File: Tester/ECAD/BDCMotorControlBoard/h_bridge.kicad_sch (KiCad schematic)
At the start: 70 parts, among them Q10 IRLR8726, Q11 IRLR8726, Q2 BC846, Q3 BC846BPN, Q4 BC846, Q5 BC846, Q6 BC846, Q7 BC846, Q8 IRLR8726, Q9 IRLR8726, U5 INA180A2, U6 IR2103, U7 IR2103

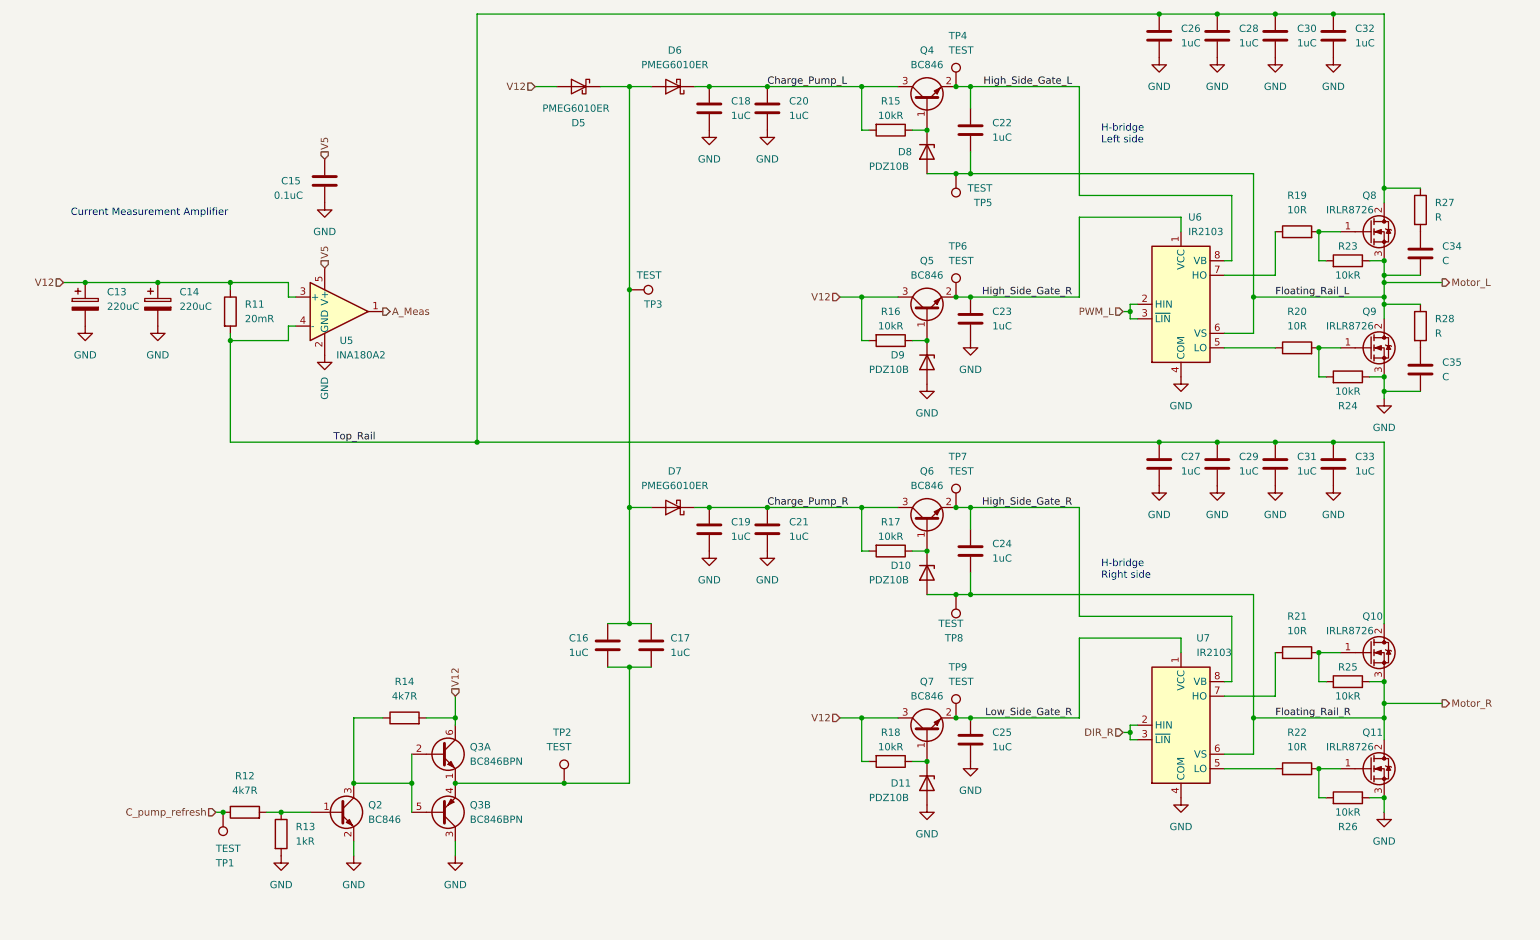
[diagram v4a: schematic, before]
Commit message: Update h_bridge.kicad_sch
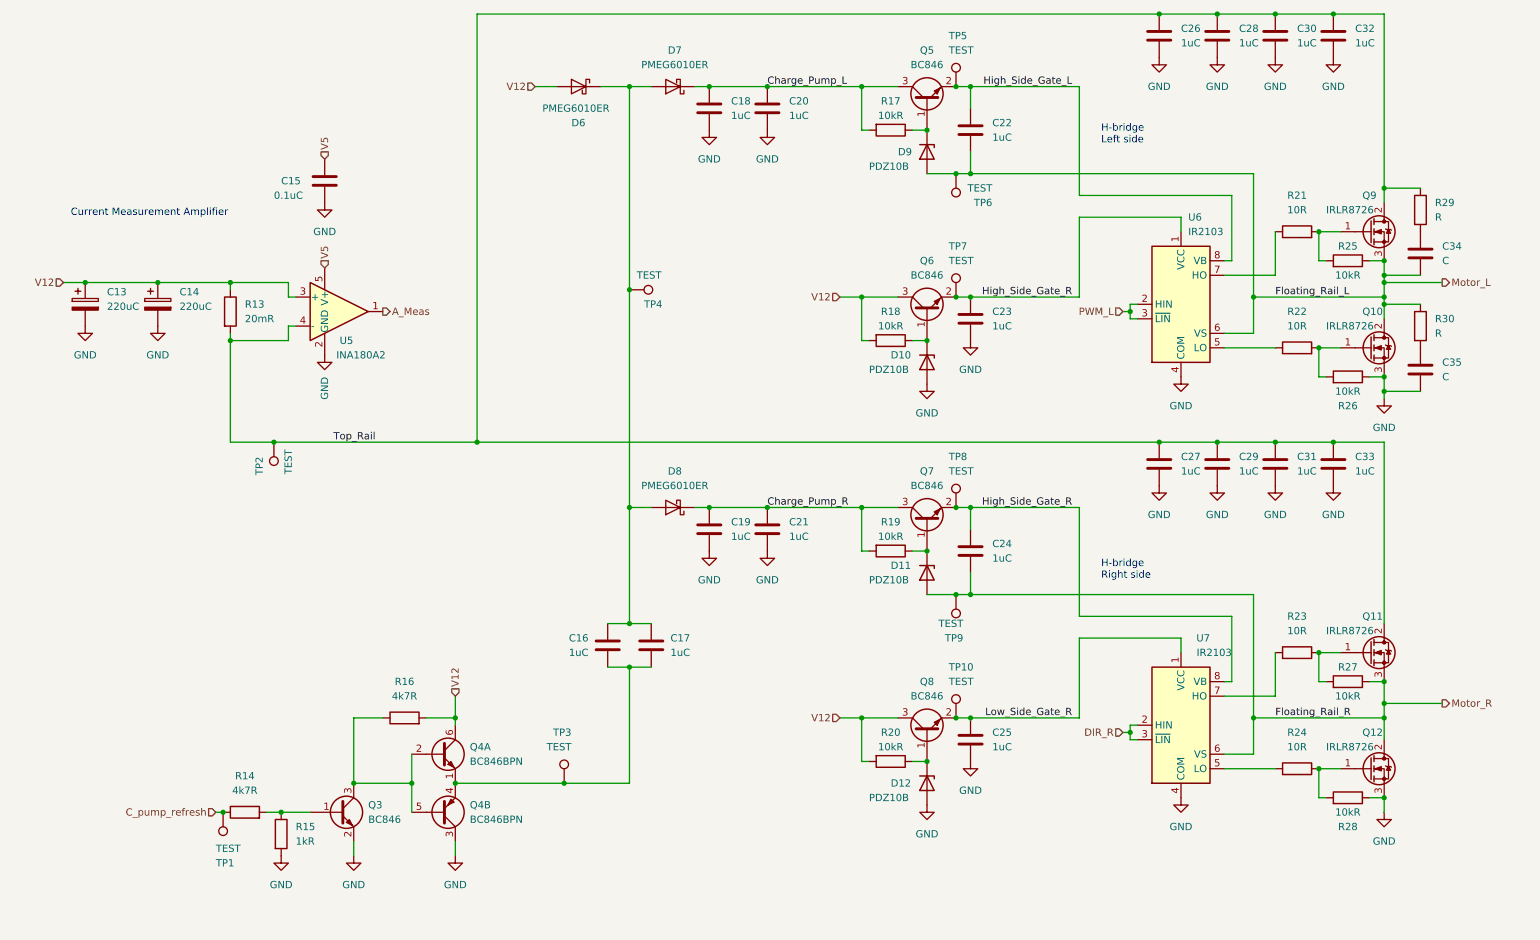
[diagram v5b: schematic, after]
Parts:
- added TP2: TEST, TestPoint:TestPoint_Pad_D1.5mm, symbol Connector:TestPoint
- renumbered D9 to D10, D10 to D11, D11 to D12, D5 to D6, D6 to D7, D7 to D8, D8 to D9, Q9 to Q10, Q10 to Q11, Q11 to Q12, Q2 to Q3, Q3 to Q4, Q4 to Q5, Q5 to Q6, Q6 to Q7, Q7 to Q8, Q8 to Q9, R11 to R13, R12 to R14, R13 to R15, R14 to R16, R15 to R17, R16 to R18, R17 to R19, R18 to R20, R19 to R21, R20 to R22, R21 to R23, R22 to R24, R23 to R25, R24 to R26, R25 to R27, R26 to R28, R27 to R29, R28 to R30, TP9 to TP10, TP2 to TP3, TP3 to TP4, TP4 to TP5, TP5 to TP6, TP6 to TP7, TP7 to TP8, TP8 to TP9
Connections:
- net Top_Rail: now also TP2.1

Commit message: Progressed CAD
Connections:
- net High_Side_Gate_R: no longer C23.1, Q6.2 (E), TP7.1, U6.1 (VCC)
- new net Low_Side_Gate_L: C23.1, Q6.2 (E), TP7.1, U6.1 (VCC)
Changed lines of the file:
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@@
     (effects (font (size 1.27 1.27)) (justify right bottom))
   )
-  (label "High_Side_Gate_R" (at 205.74 67.31 180)
+  (label "Low_Side_Gate_L" (at 205.74 67.31 180)
     (effects (font (size 1.27 1.27)) (justify right bottom))
-  )
-  (label "Floating_Rail_L" (at 241.3 67.31 0)
-    (effects (font (size 1.27 1.27)) (justify left bottom))
   )
   (label "Low_Side_Gate_R" (at 205.74 140.97 180)
@@
     (effects (font (size 1.27 1.27)) (justify left bottom))
   )
-  (label "Floating_Rail_R" (at 241.3 140.97 0)
-    (effects (font (size 1.27 1.27)) (justify left bottom))
-  )

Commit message: Progressed CAD
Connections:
- net Top_Rail: now also C13.1, C14.1
- net V12: no longer C13.1, C14.1
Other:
- moved on the sheet: C13, C14, TP2

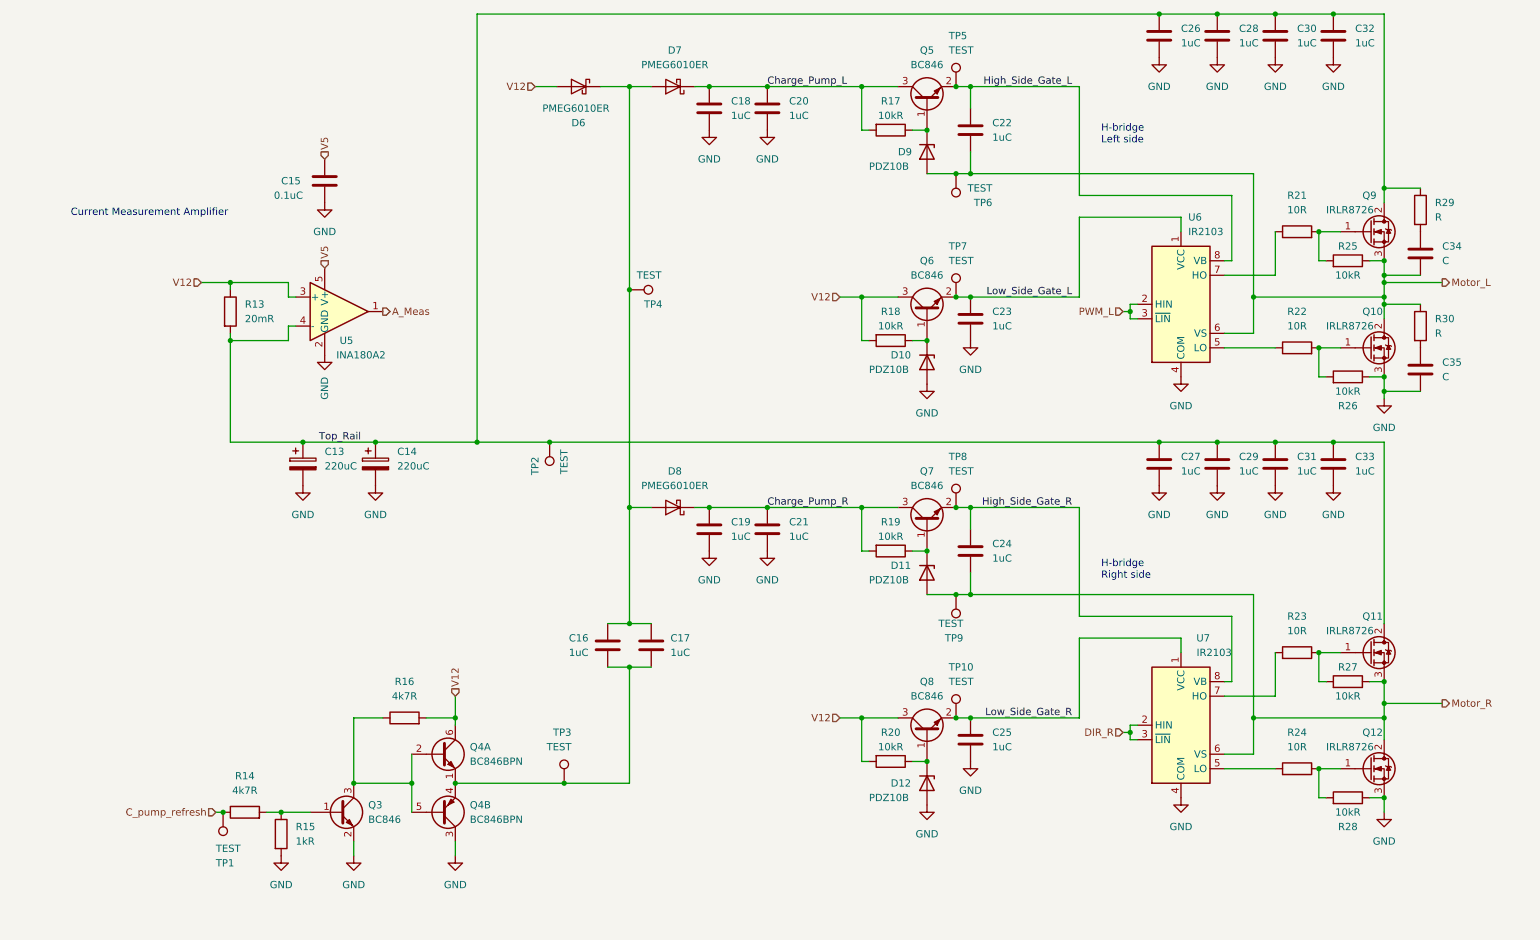
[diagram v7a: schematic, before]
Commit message: Update h_bridge.kicad_sch
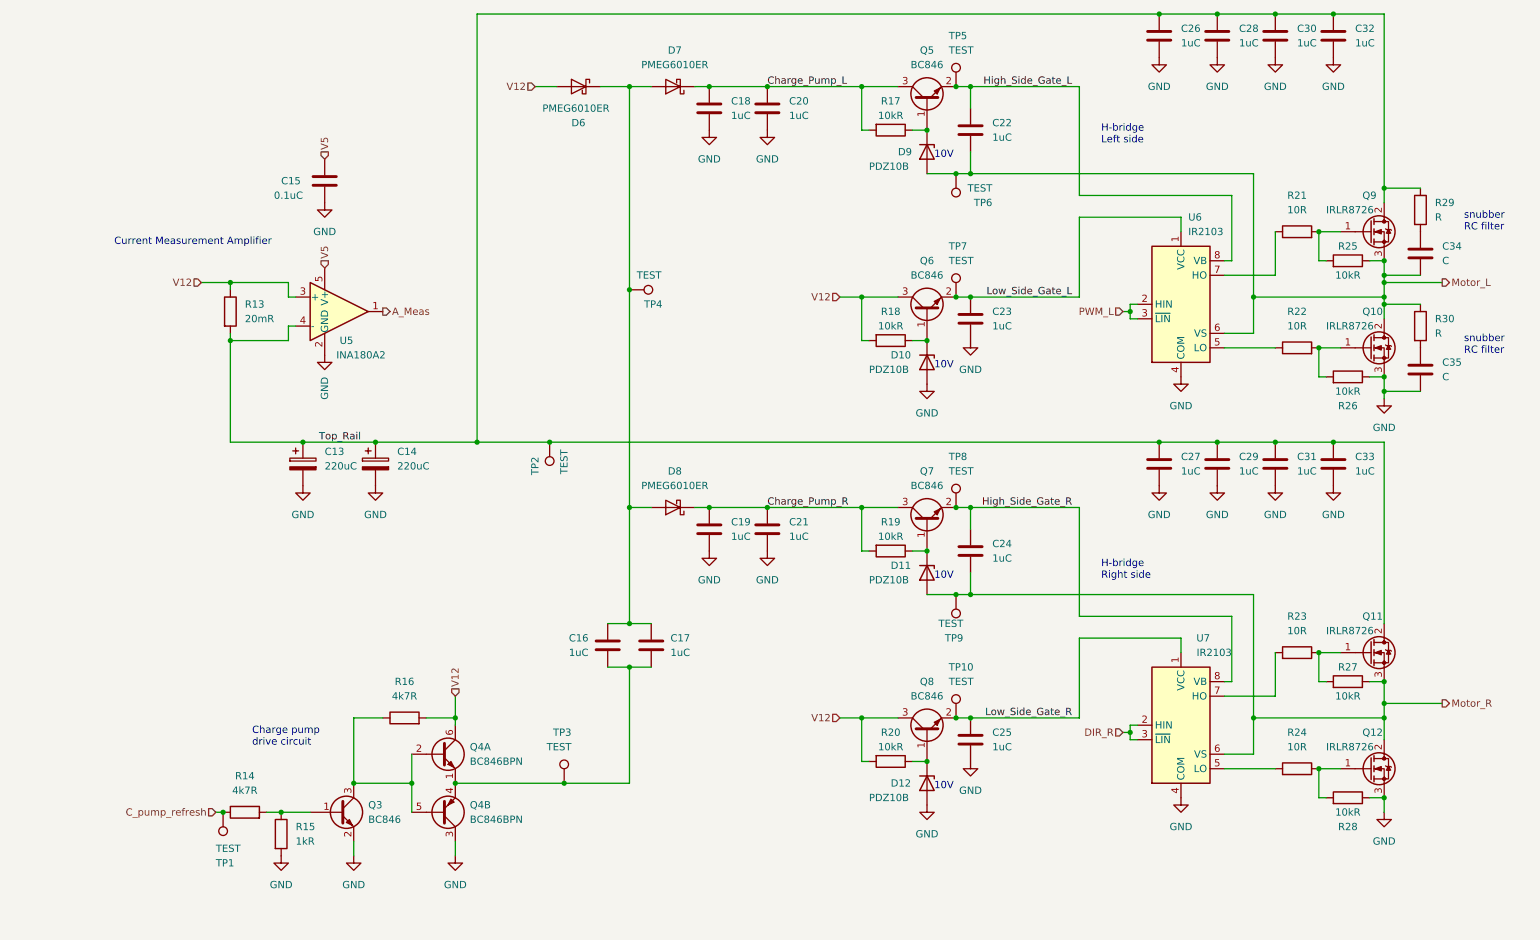
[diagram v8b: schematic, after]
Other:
- note added: "10V"
- note added: "Charge pump drive circuit"
- note added: "snubber RC filter"
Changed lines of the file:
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@@
     (stroke (width 0) (type default) (color 0 0 0 0))
+  )
+  (text "snubber\nRC filter" (at 274.32 55.88 0)
+    (effects (font (size 1.27 1.27)) (justify left bottom))
+  )
+  (text "Charge pump\ndrive circuit" (at 62.23 146.05 0)
+    (effects (font (size 1.27 1.27)) (justify left bottom))
+  )
+  (text "10V" (at 181.61 43.18 0)
+    (effects (font (size 1.27 1.27)) (justify left bottom))
+  )
+  (text "10V" (at 181.61 153.67 0)
+    (effects (font (size 1.27 1.27)) (justify left bottom))
   )
   (text "H-bridge\nRight side" (at 210.82 116.84 0)
     (effects (font (size 1.27 1.27)) (justify left bottom))
   )
-  (text "Current Measurement Amplifier" (at 30.48 53.34 0)
+  (text "10V" (at 181.61 80.01 0)
+    (effects (font (size 1.27 1.27)) (justify left bottom))
+  )
+  (text "Current Measurement Amplifier" (at 38.1 58.42 0)
+    (effects (font (size 1.27 1.27)) (justify left bottom))
+  )
+  (text "snubber\nRC filter" (at 274.32 77.47 0)
     (effects (font (size 1.27 1.27)) (justify left bottom))
   )
@@
     (effects (font (size 1.27 1.27)) (justify left bottom))
   )
+  (text "10V" (at 181.61 116.84 0)
+    (effects (font (size 1.27 1.27)) (justify left bottom))
+  )
